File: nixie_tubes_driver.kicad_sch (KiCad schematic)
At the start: 3 parts, among them U5 CD40109BPW, U6 HV5122PG-G, U7 HV5122PG-G

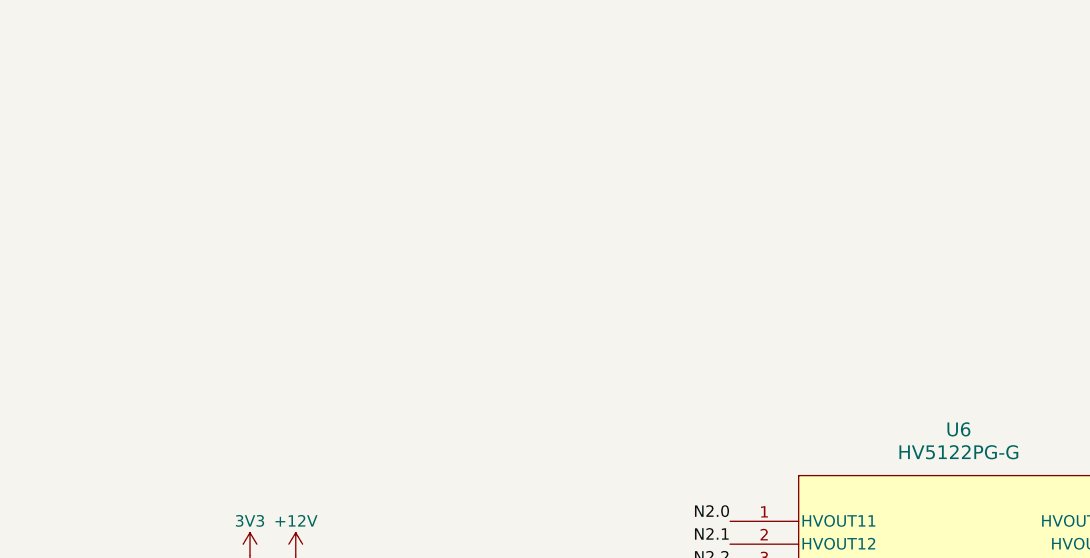
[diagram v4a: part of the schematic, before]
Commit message: Add 12V boost converter
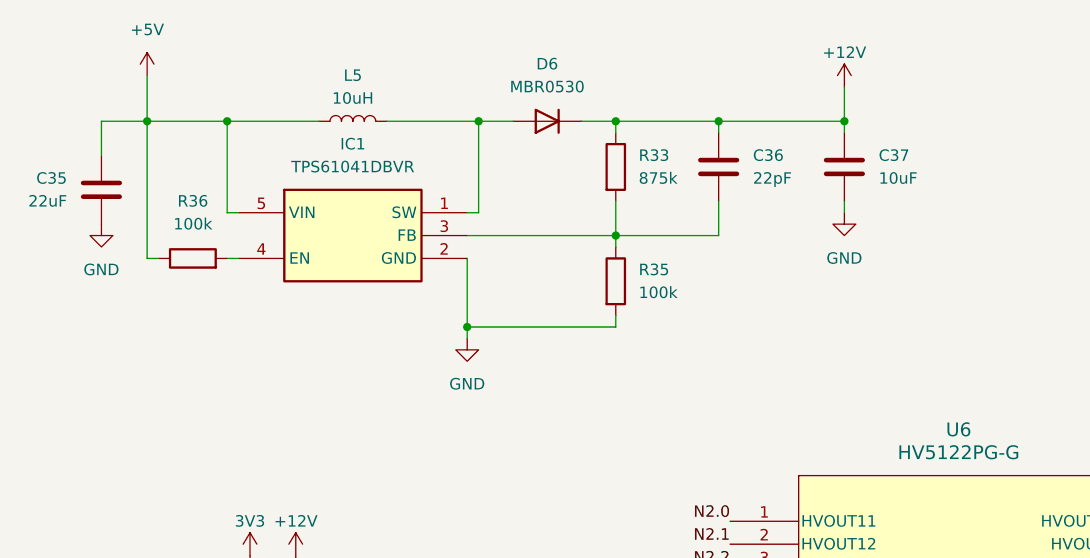
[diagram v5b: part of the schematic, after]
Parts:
- added C35: 22uF, Capacitor_SMD:C_0805_2012Metric, symbol Device:C
- added C36: 22pF, Capacitor_SMD:C_0603_1608Metric, symbol Device:C
- added C37: 10uF, Capacitor_SMD:C_1206_3216Metric, symbol Device:C
- added D6: MBR0530, Diode_SMD:D_SOD-123, symbol Device:D
- added IC1: TPS61041DBVR, eclectronics_nixie_footprints:SOT95P280X145-5N, symbol eclectronics_nixie_lib:TPS61041DBVR Boost Converter (250mA)
- added L5: 10uH, Inductor_SMD:L_1008_2520Metric, symbol Device:L
- added R33: 875k, Resistor_SMD:R_0603_1608Metric, symbol Device:R
- added R35, R36: 100k, Resistor_SMD:R_0603_1608Metric, symbol Device:R
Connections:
- net +12V: now also C36.1, C37.1, D6.1 (K), R33.1
- net GND: now also C35.2, C37.2, IC1.2 (GND), R35.2
- new net: C36.2, IC1.3 (FB), R33.2, R35.1
- new net: D6.2 (A), IC1.1 (SW), L5.2
- new net: IC1.4 (EN), R36.2
- new net +5V: C35.1, IC1.5 (VIN), L5.1, R36.1

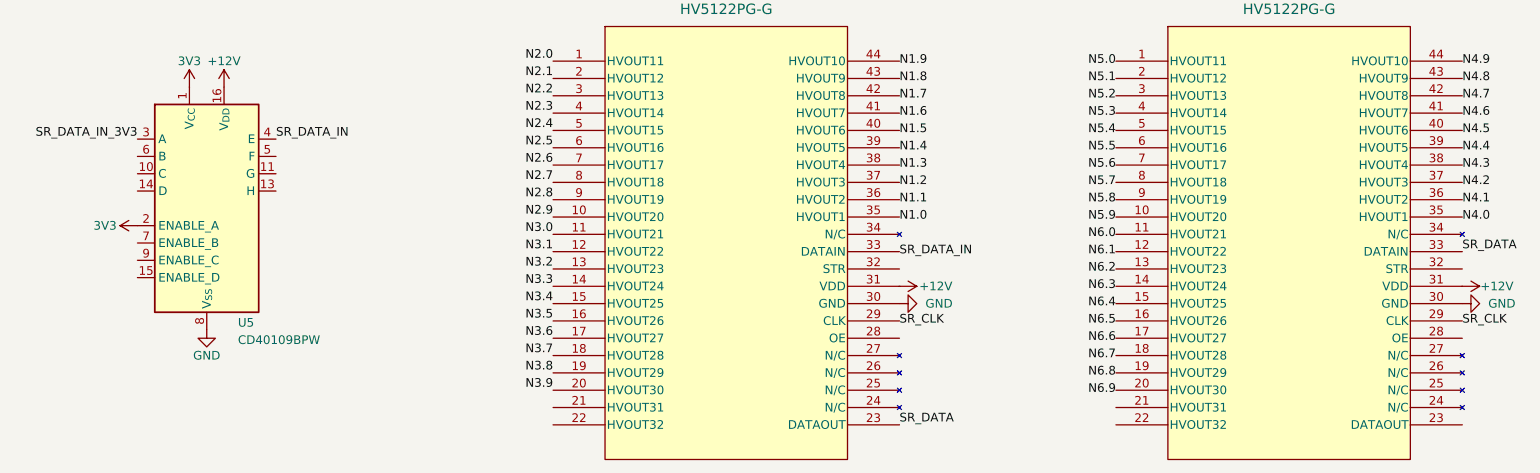
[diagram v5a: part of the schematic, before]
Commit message: Add data connections between driver and rp2350
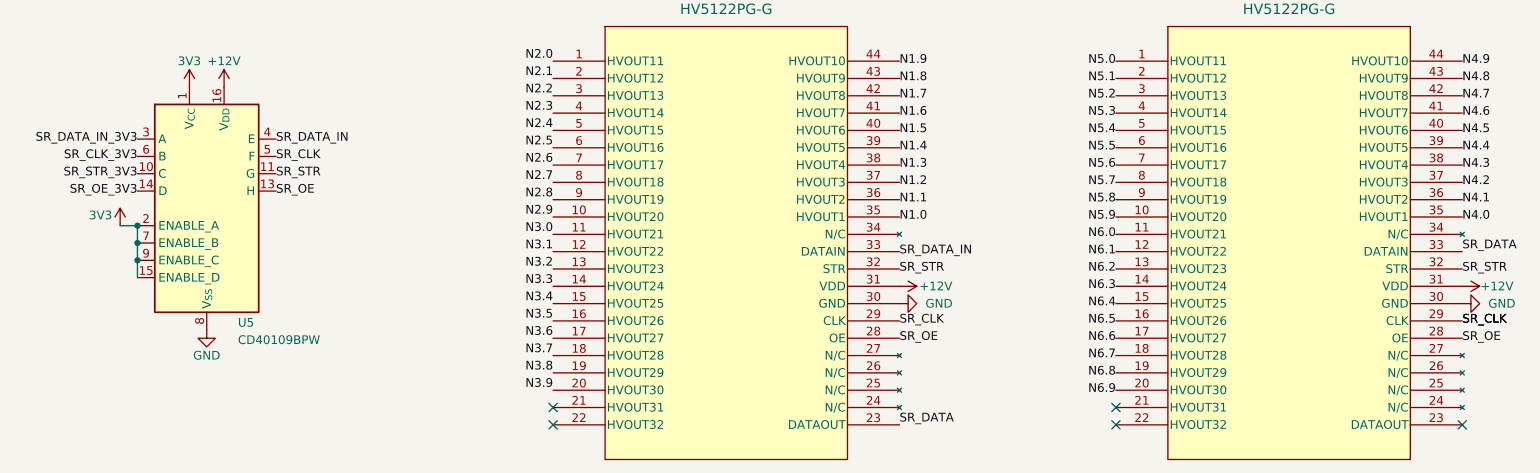
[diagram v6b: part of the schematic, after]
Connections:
- net 3V3: now also U5.15 (ENABLE_D), U5.7 (ENABLE_B), U5.9 (ENABLE_C)
- net SR_CLK: now also U5.5 (F)
- net SR_OE: now reaches U6.28 (OE)
- net SR_OE: now also U5.13 (H), U7.28 (OE)
- net SR_STR: now reaches U6.32 (STR)
- net SR_STR: now also U5.11 (G), U7.32 (STR)
- net SR_STR_3V3: now reaches U5.10 (C)
- net SR_OE_3V3: now reaches U5.14 (D)
- net SR_CLK_3V3: now reaches U5.6 (B)
- no-connect marks 0 -> 5
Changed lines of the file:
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@@
 	(paper "A4")
+	(junction
+		(at 33.02 104.14)
+		(diameter 0)
+		(color 0 0 0 0)
+	)
 	(junction
 		(at 106.68 33.02)
@@
 	)
 	(junction
+		(at 33.02 106.68)
+		(diameter 0)
+		(color 0 0 0 0)
+	)
+	(junction
 		(at 64.77 55.88)
 		(diameter 0)
@@
 	)
 	(junction
+		(at 33.02 101.6)
+		(diameter 0)
+		(color 0 0 0 0)
+	)
+	(junction
 		(at 81.28 33.02)
 		(diameter 0)
 		(color 0 0 0 0)
 	)
+	(no_connect
+		(at 93.98 128.27)
+	)
+	(no_connect
+		(at 227.33 130.81)
+	)
+	(no_connect
+		(at 93.98 130.81)
+	)
+	(no_connect
+		(at 176.53 128.27)
+	)
+	(no_connect
+		(at 176.53 130.81)
+	)
 	(wire
 		(pts
@@
 	(wire
 		(pts
+			(xy 33.02 106.68) (xy 33.02 109.22)
+		)
+		(stroke
+			(width 0)
+			(type default)
+		)
+	)
+	(wire
+		(pts
 			(xy 106.68 43.18) (xy 106.68 41.91)
 		)
@@
 	(wire
 		(pts
+			(xy 33.02 104.14) (xy 33.02 106.68)
+		)
+		(stroke
+			(width 0)
+			(type default)
+		)
+	)
+	(wire
+		(pts
 			(xy 66.04 33.02) (xy 55.88 33.02)
 		)
@@
 	(wire
 		(pts
+			(xy 33.02 101.6) (xy 33.02 104.14)
+		)
+		(stroke
+			(width 0)
+			(type default)
+		)
+	)
+	(wire
+		(pts
 			(xy 38.1 43.18) (xy 39.37 43.18)
 		)
@@
 		(pts
 			(xy 92.71 41.91) (xy 92.71 45.72)
+		)
+		(stroke
+			(width 0)
+			(type default)
+		)
+	)
+	(wire
+		(pts
+			(xy 30.48 101.6) (xy 33.02 101.6)
 		)
 		(stroke
@@
 		)
 	)
+	(label "SR_OE"
+		(at 144.78 118.11 0)
+		(effects
+			(font
+				(size 1.27 1.27)
+			)
+			(justify left)
+		)
+	)
 	(label "N6.1"
 		(at 176.53 105.41 180)
@@
 				(size 1.27 1.27)
 			)
-			(justify left bottom)
+			(justify left)
 		)
 	)
@@
 		)
 	)
+	(label "SR_STR"
+		(at 53.34 93.98 0)
+		(effects
+			(font
+				(size 1.27 1.27)
+			)
+			(justify left)
+		)
+	)
 	(label "N5.4"
 		(at 176.53 87.63 180)
@@
 		)
 	)
+	(label "SR_CLK"
+		(at 227.33 115.57 0)
+		(effects
+			(font
+				(size 1.27 1.27)
+			)
+			(justify left)
+		)
+	)
 	(label "N3.1"
 		(at 93.98 105.41 180)
@@
 		)
 	)
+	(label "SR_OE_3V3"
+		(at 33.02 96.52 180)
+		(effects
+			(font
+				(size 1.27 1.27)
+			)
+			(justify right)
+		)
+	)
 	(label "N1.5"
 		(at 144.78 87.63 0)
@@
 		)
 	)
+	(label "SR_STR_3V3"
+		(at 33.02 93.98 180)
+		(effects
+			(font
+				(size 1.27 1.27)
+			)
+			(justify right)
+		)
+	)
 	(label "N6.9"
 		(at 176.53 125.73 180)
@@
 				(size 1.27 1.27)
 			)
-			(justify right bottom)
+			(justify right)
 		)
 	)
@@
 		)
 	)
+	(label "SR_OE"
+		(at 227.33 118.11 0)
+		(effects
+			(font
+				(size 1.27 1.27)
+			)
+			(justify left)
+		)
+	)
+	(label "SR_CLK"
+		(at 53.34 91.44 0)
+		(effects
+			(font
+				(size 1.27 1.27)
+			)
+			(justify left)
+		)
+	)
 	(label "SR_DATA"
 		(at 144.78 130.81 0)
@@
 		)
 	)
+	(label "SR_STR"
+		(at 144.78 107.95 0)
+		(effects
+			(font
+				(size 1.27 1.27)
+			)
+			(justify left)
+		)
+	)
 	(label "N6.7"
 		(at 176.53 120.65 180)
@@
 		)
 	)
+	(label "SR_STR"
+		(at 227.33 107.95 0)
+		(effects
+			(font
+				(size 1.27 1.27)
+			)
+			(justify left)
+		)
+	)
 	(label "N4.2"
 		(at 227.33 95.25 0)
@@
 		)
 	)
+	(label "SR_CLK_3V3"
+		(at 33.02 91.44 180)
+		(effects
+			(font
+				(size 1.27 1.27)
+			)
+			(justify right)
+		)
+	)
 	(label "N6.3"
 		(at 176.53 110.49 180)
@@
 		)
 	)
+	(label "SR_OE"
+		(at 53.34 96.52 0)
+		(effects
+			(font
+				(size 1.27 1.27)
+			)
+			(justify left)
+		)
+	)
 	(symbol
 		(lib_id "power:+5V")
-		(at 33.02 101.6 90)
+		(at 30.48 101.6 0)
 		(unit 1)
 		(exclude_from_sim no)
@@
 		(dnp no)
 		(property "Reference" "#PWR089"
-			(at 36.83 101.6 0)
+			(at 30.48 105.41 0)
 			(effects
 				(font
@@
 		)
 		(property "Value" "3V3"
-			(at 29.972 101.6 90)
+			(at 25.908 100.076 0)
 			(effects
 				(font
@@
 		)
 		(property "Footprint" ""
-			(at 33.02 101.6 0)
+			(at 30.48 101.6 0)
 			(effects
 				(font
@@
 		)
 		(property "Datasheet" ""
-			(at 33.02 101.6 0)
+			(at 30.48 101.6 0)
 			(effects
 				(font
@@
 		)
 		(property "Description" "Power symbol creates a global label with name \"+5V\""
-			(at 33.02 101.6 0)
+			(at 30.48 101.6 0)
 			(effects
 				(font

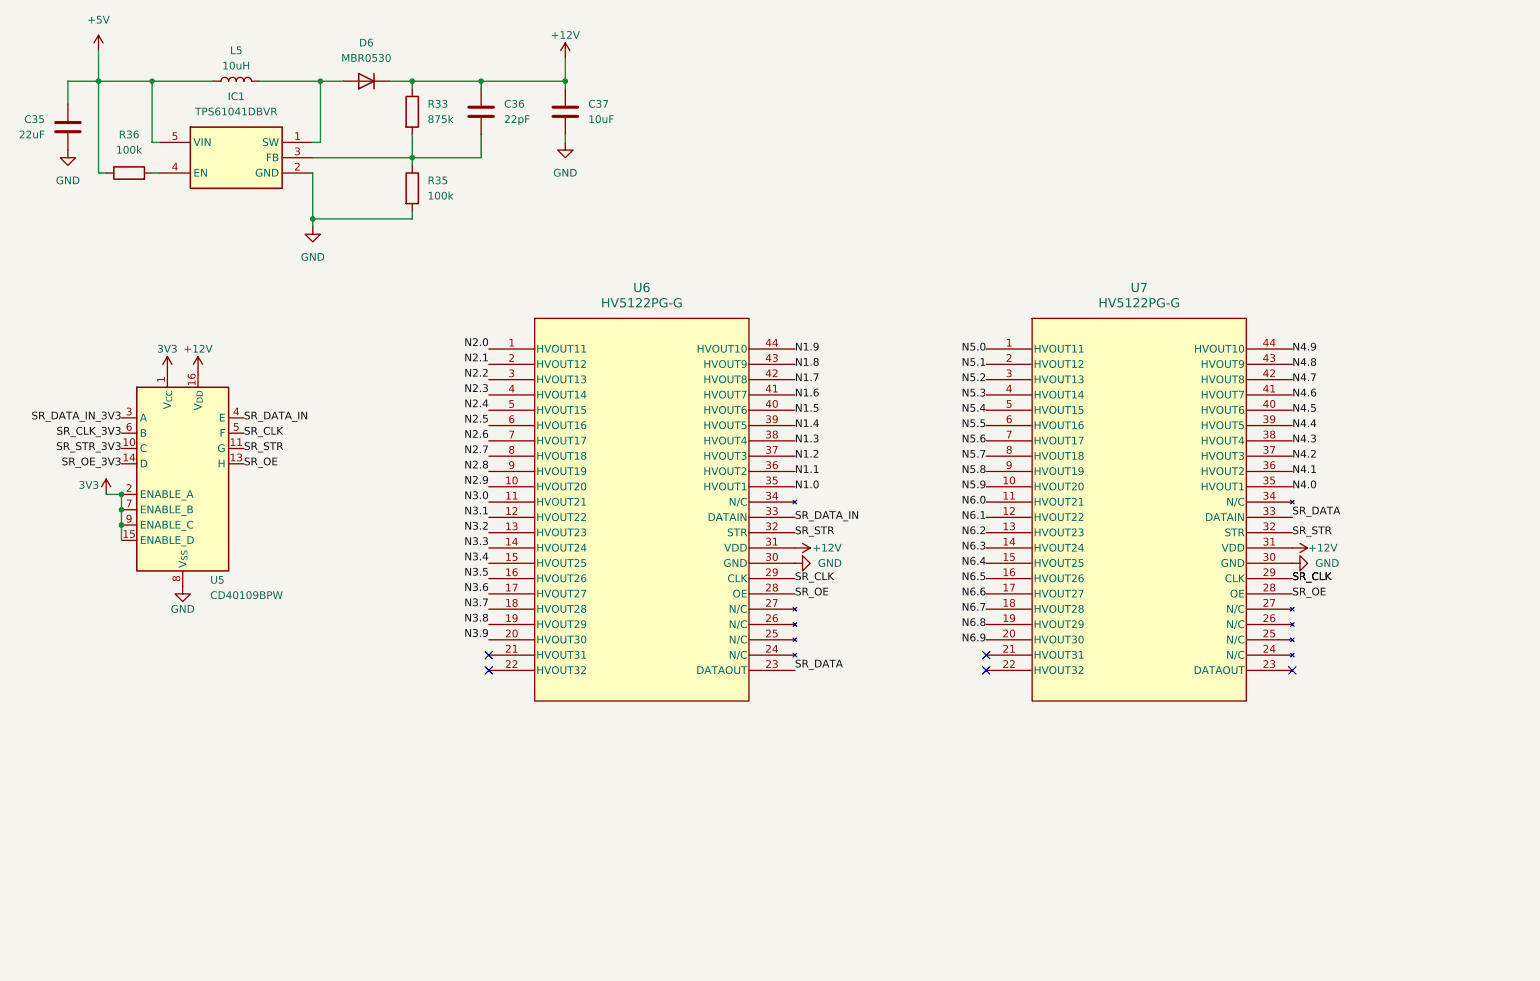
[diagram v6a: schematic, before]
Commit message: Update power supply layout and add associated components
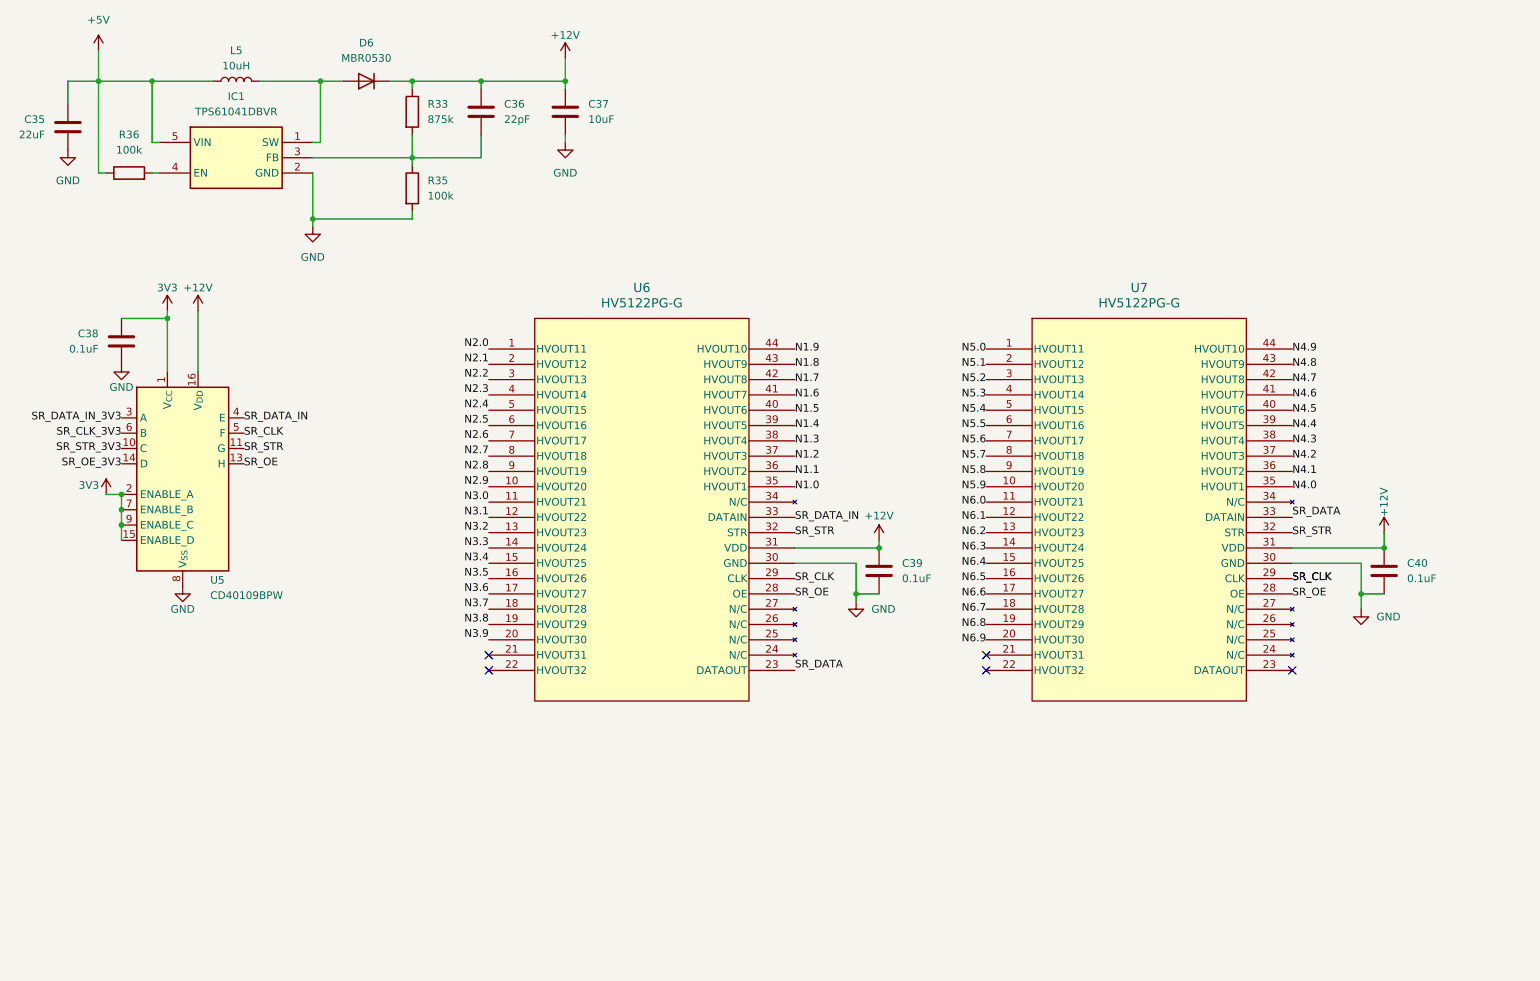
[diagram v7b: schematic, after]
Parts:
- added C38, C39, C40: 0.1uF, Capacitor_SMD:C_0603_1608Metric, symbol Device:C
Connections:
- net +12V: now also C39.1, C40.1
- net 3V3: now also C38.1
- net GND: now also C38.2, C39.2, C40.2

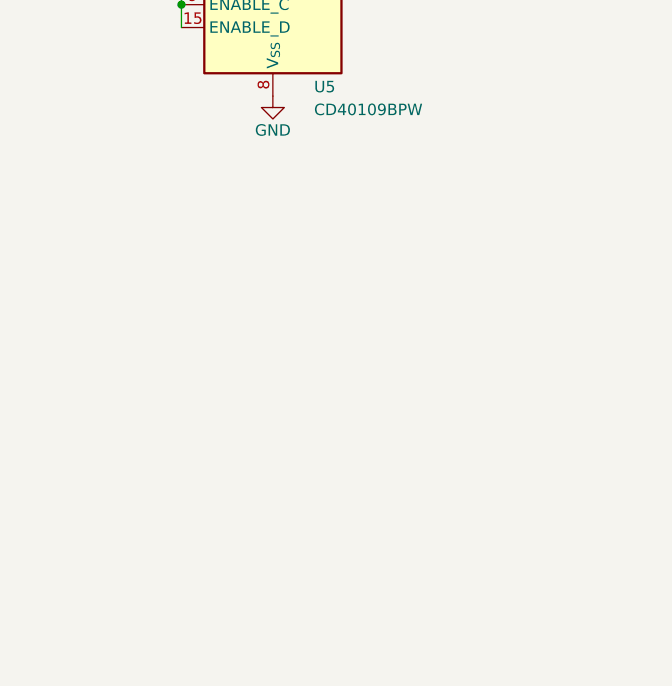
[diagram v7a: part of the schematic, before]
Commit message: Add backlight LEDs
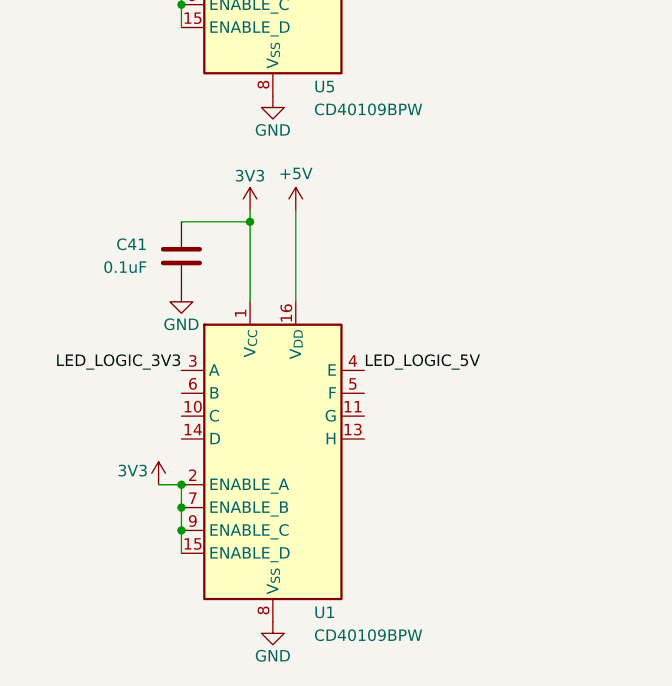
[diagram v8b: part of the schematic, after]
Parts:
- added C41: 0.1uF, Capacitor_SMD:C_0603_1608Metric, symbol Device:C
- added U1: CD40109BPW, Package_SO:TSSOP-16_4.4x5mm_P0.65mm, symbol Logic_LevelTranslator:CD40109BPW
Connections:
- net +5V: now also U1.16 (V_{DD})
- net 3V3: now also C41.1, U1.1 (V_{CC}), U1.15 (ENABLE_D), U1.2 (ENABLE_A), U1.7 (ENABLE_B), U1.9 (ENABLE_C)
- net GND: now also C41.2, U1.8 (V_{SS})
- new net LED_LOGIC_3V3: U1.3 (A)
- new net LED_LOGIC_5V: U1.4 (E)
